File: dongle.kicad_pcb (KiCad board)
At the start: 2 copper layers, 67 x 77 mm, 90 parts, among them J1 AudioJack2_Ground_Switch, J2 AudioJack2_Ground_Switch, J3 AudioJack2_Ground_Switch, J4 AudioJack2_Ground_Switch, J5 AudioJack2_Ground_Switch, P1 Digital, P4 Analog, Q1 MMBT3904, Q10 MMBT3904, Q11 MMBT3904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

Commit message: Change the footprints on the LED's to indicate which pad is for the cathode so that they can be soldered more easily.
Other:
- board text added: "REV: 1a"
- board text removed: "REV: 1"

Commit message: Fix an error in the schematic and update the PC board layout.
The emitter of Q16 needs to be grounded or port 3's red LED doesn't work.
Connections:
- Q16 pad 2: Net-(Q16-Pad2) -> GND
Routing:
- net GND: vias 10 -> 11
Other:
- board text added: "REV: 2a"
- board text removed: "REV: 1a"

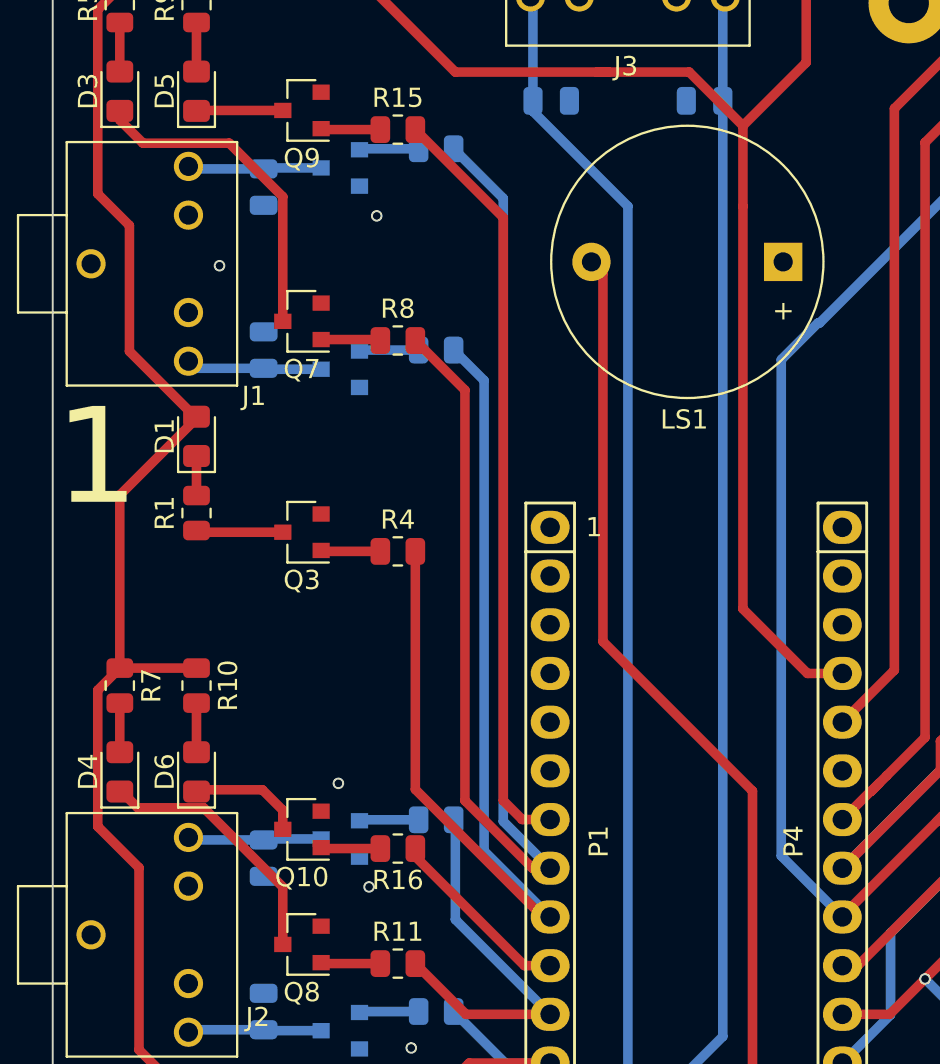
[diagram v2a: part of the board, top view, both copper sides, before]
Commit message: While I'm at it, I can also fix the footprint of the buzzer, which doesn't match the parts I actually have, and fix another issue when I ran a DRC
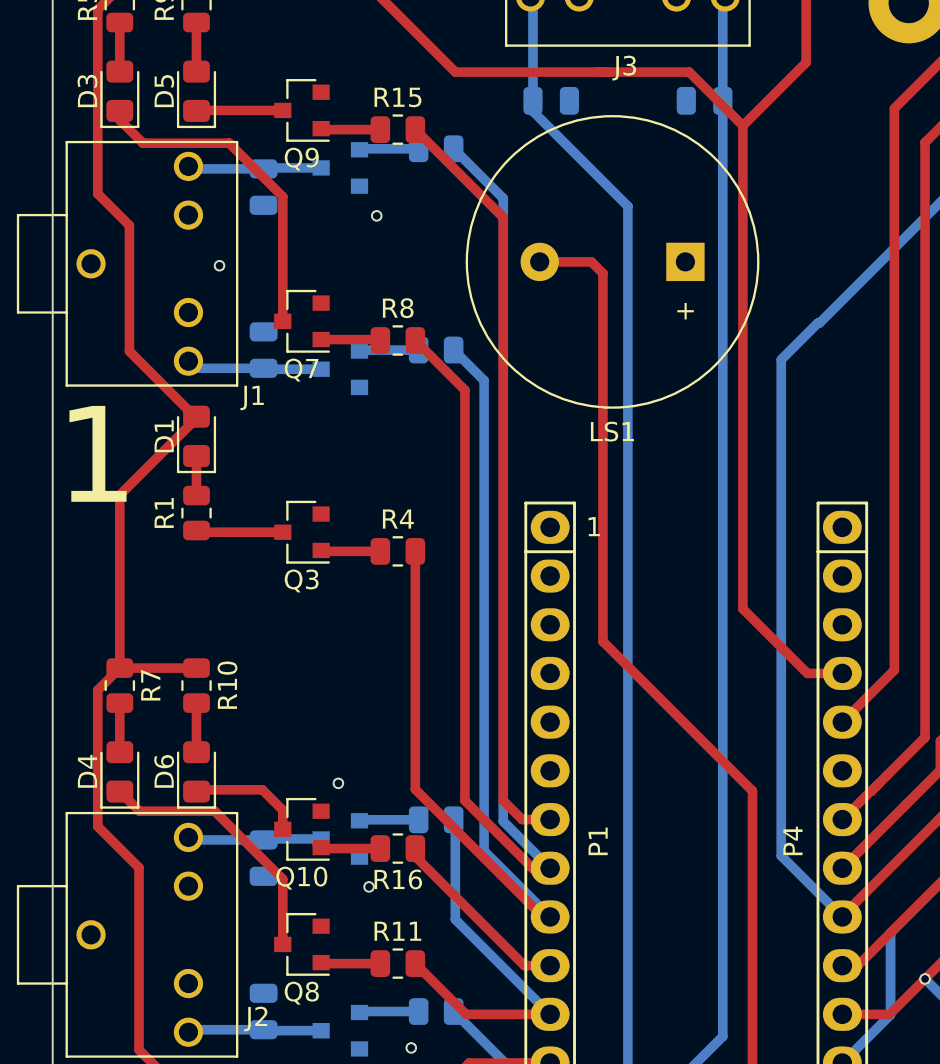
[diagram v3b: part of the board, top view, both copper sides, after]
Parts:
- LS1: footprint Buzzer_Beeper:Buzzer_D14mm_H7mm_P10mm -> Buzzer_Beeper:Buzzer_15x7.5RM7.6
- moved LS1 5.10 mm to (146.5, 57.4)
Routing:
- net Net-(LS1-Pad2): track 57.5 -> 59.7 mm
